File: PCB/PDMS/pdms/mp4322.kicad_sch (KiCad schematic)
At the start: 17 parts, among them U7 MP4322GDE-P

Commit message: WIP PCB folder structure and schematic clean-up
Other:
- company: (none) -> PGRacing Team
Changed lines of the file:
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@@
 (kicad_sch (version 20211123) (generator eeschema)
   (paper "A4")
+  (title_block
+    (rev "V4.2")
+    (company "PGRacing Team")
+    (comment 1 "Karol Pergoł")
+  )
   (junction (at 106.68 83.185) (diameter 0) (color 0 0 0 0)
   )

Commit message: PDMS PCB input modification WIP - no supply
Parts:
- C25, C26: value 0.1uF -> 100nF

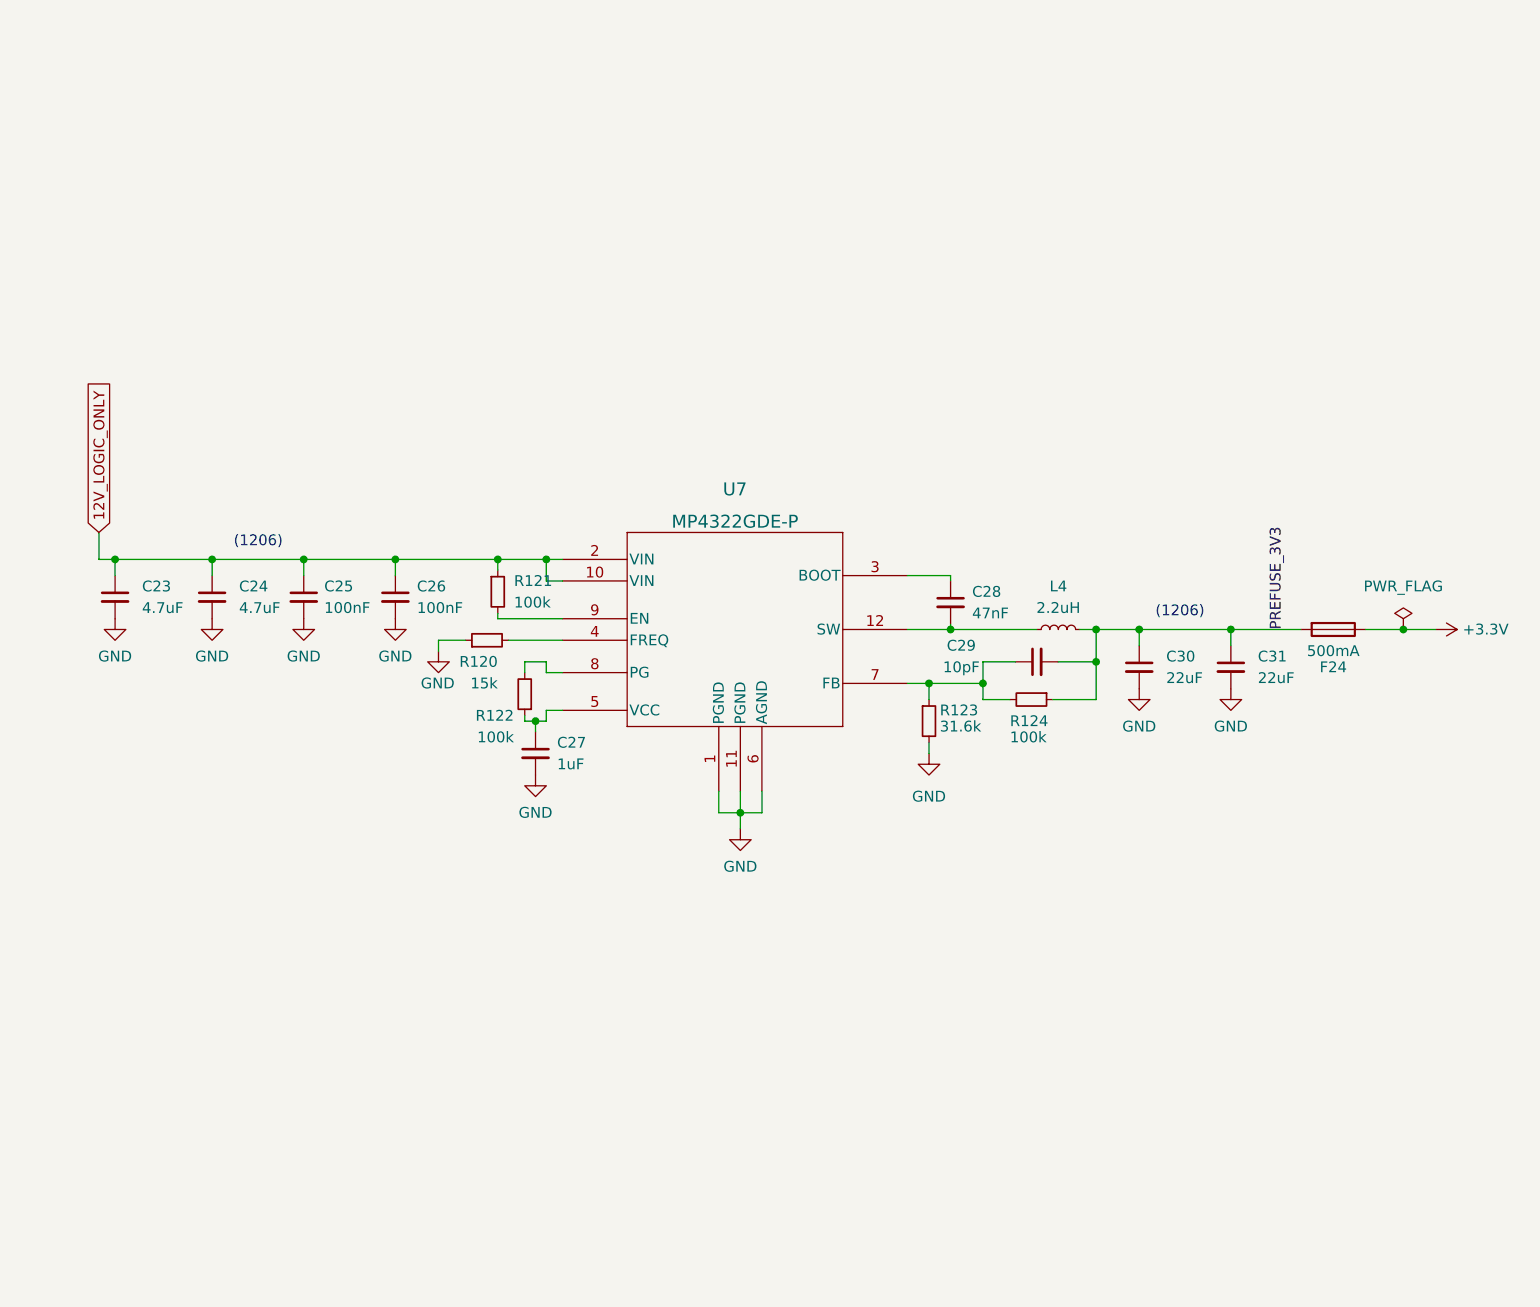
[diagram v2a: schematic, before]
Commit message: Fixed memory and aux routing, fixed decoupling of MCU, fixed hse oscilator layout, fixed BTS500 input capacitors size and thermal, fixed via stiching on output channels, changed LP mos  traces to thiner ones, WIP mp4322 layout repliacte
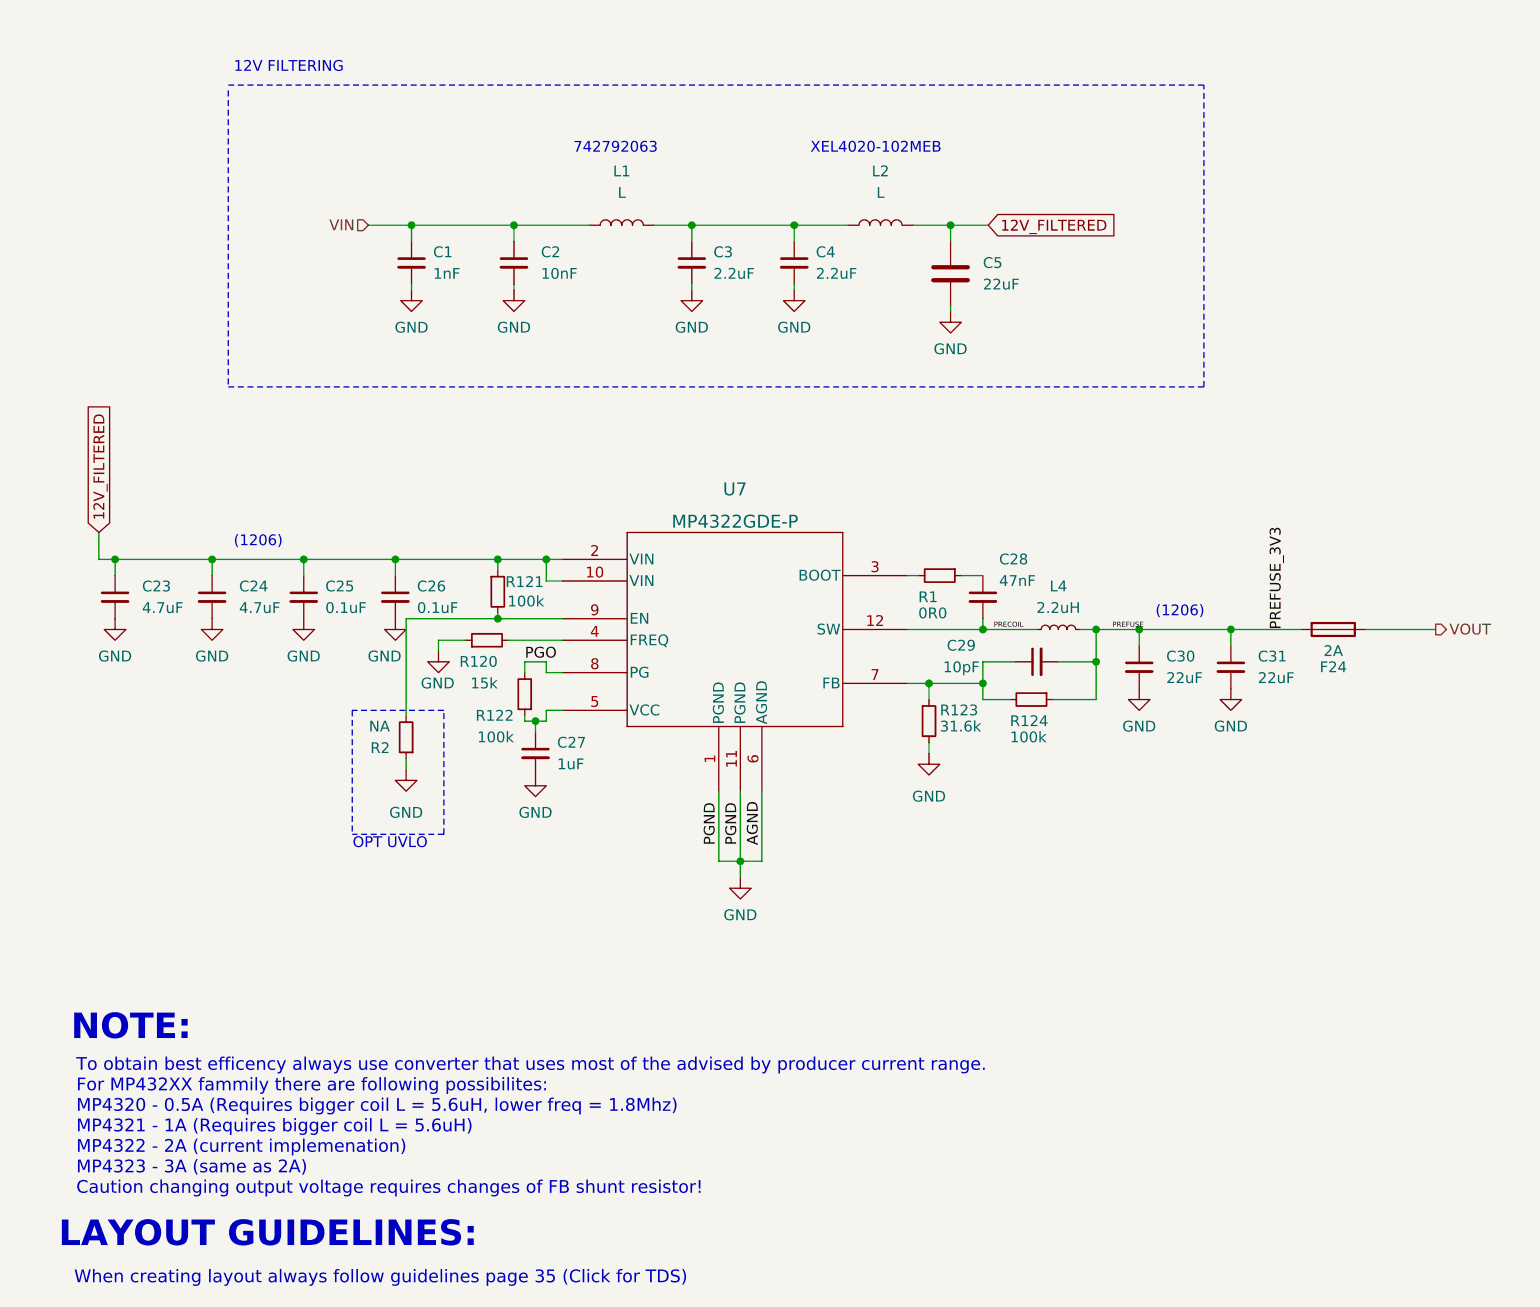
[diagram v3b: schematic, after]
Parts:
- added C1: 1nF, Capacitor_SMD:C_0402_1005Metric, symbol Device:C_Small
- added C2: 10nF, Capacitor_SMD:C_0402_1005Metric, symbol Device:C_Small
- added C3, C4: 2.2uF, Capacitor_SMD:C_0805_2012Metric, symbol Device:C_Small
- added C5: 22uF, Capacitor_SMD:CP_Elec_6.3x9.9, symbol Device:C
- added L1: L, Inductor_SMD:L_0805_2012Metric, symbol Device:L
- added L2: L, Inductor_SMD:L_Coilcraft_XxL4020, symbol Device:L
- added R1: 0R0, Resistor_SMD:R_0402_1005Metric, symbol Device:R_Small
- added R2: NA, Resistor_SMD:R_0402_1005Metric, symbol Device:R_Small
- C25, C26: value 100nF -> 0.1uF
- C27, C28, C29: footprint Resistor_SMD:R_0402_1005Metric -> Capacitor_SMD:C_0402_1005Metric
- F24: value 500mA -> 2A
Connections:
- net GND: now also C1.2, C2.2, C3.2, C4.2, C5.2, R2.1
- net PGO: now reaches R122.2, U7.8 (PG)
- net at R121.2, U7.9 (EN): now also R2.2
- net PRECOIL: now reaches C28.2, L4.1, U7.12 (SW)
- net at U7.3 (BOOT): now also R1.2; no longer C28.1
- net +3.3V renamed VOUT
- net 12V_LOGIC_ONLY renamed 12V_FILTERED
- net 12V_FILTERED: now also C5.1, L2.1
- net PREFUSE_3V3 renamed PREFUSE
- new net: C3.1, C4.1, L1.2, L2.2
- new net: C28.1, R1.1
- new net VIN: C1.1, C2.1, L1.1
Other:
- note added: "12V FILTERING"
- note added: "742792063"
- note added: "LAYOUT GUIDELINES:"
- note added: "NOTE:"
- note added: "OPT UVLO"
- note added: "To obtain best efficency always use converter that uses most of the advised by producer current range. For MP432XX fammily there are following possibilites: MP4320 - 0.5A (Requires bigger coil L = 5.6uH, lower freq = 1.8Mhz) MP4321 - 1A (Requires bigger coil L = 5.6uH) MP4322 - 2A (current implemenation) MP4323 - 3A (same as 2A) Caution changing output voltage requires changes of FB shunt resisto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"
- note added: "When creating layout always follow guidelines page 35 (Click for TDS)"
- note added: "XEL4020-102MEB"
- title: (none) -> MP432X Power section
- moved on the sheet: C28

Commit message: PDMS PCB WIP modification mp4322 finished layput, cleared USB-C layout, moved OSC32 for better fit
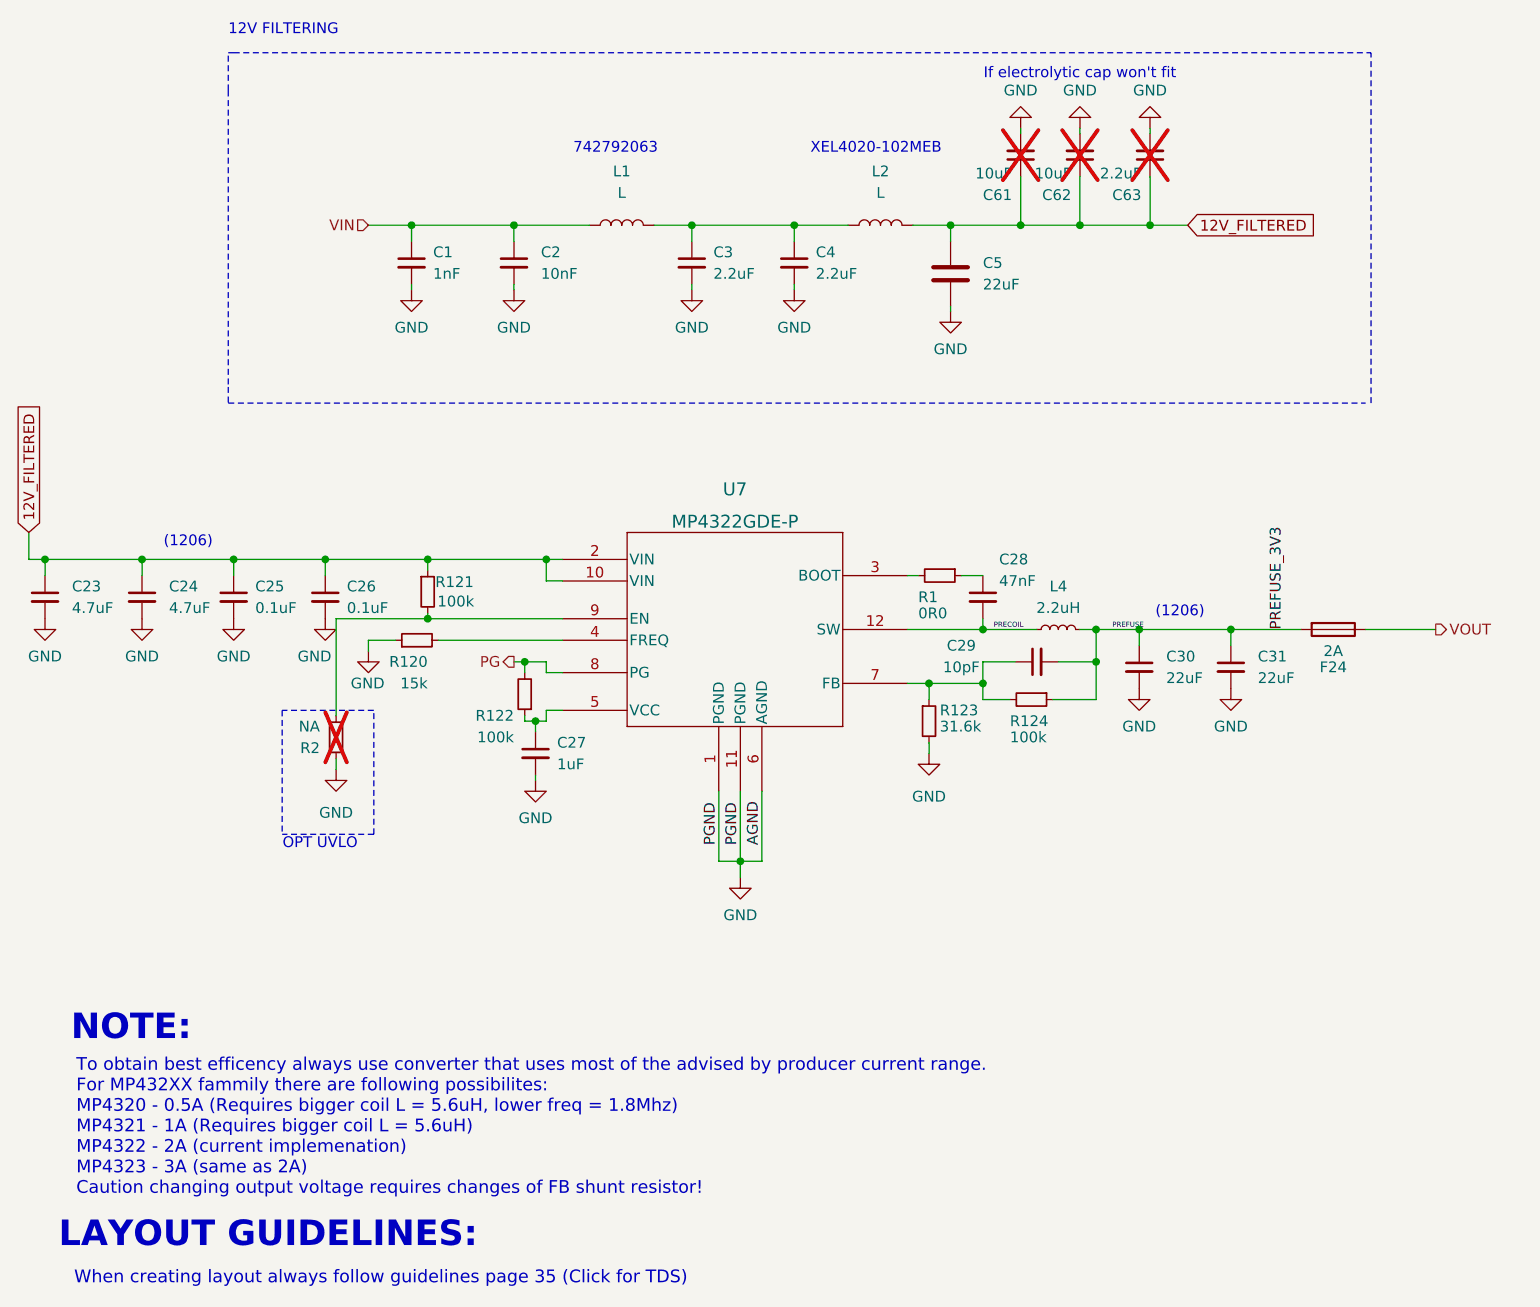
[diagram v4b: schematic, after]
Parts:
- added C61, C62: 10uF, Capacitor_SMD:C_1206_3216Metric, symbol Device:C_Small
- added C63: 2.2uF, Capacitor_SMD:C_1206_3216Metric, symbol Device:C_Small
- R2: now not fitted
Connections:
- net 12V_FILTERED: now also C61.1, C62.1, C63.1
- net GND: now also C61.2, C62.2, C63.2
- net PGO renamed PG
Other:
- note added: "If electrolytic cap won't fit"
- moved on the sheet: C23, C24, C25, C26, R120, R121

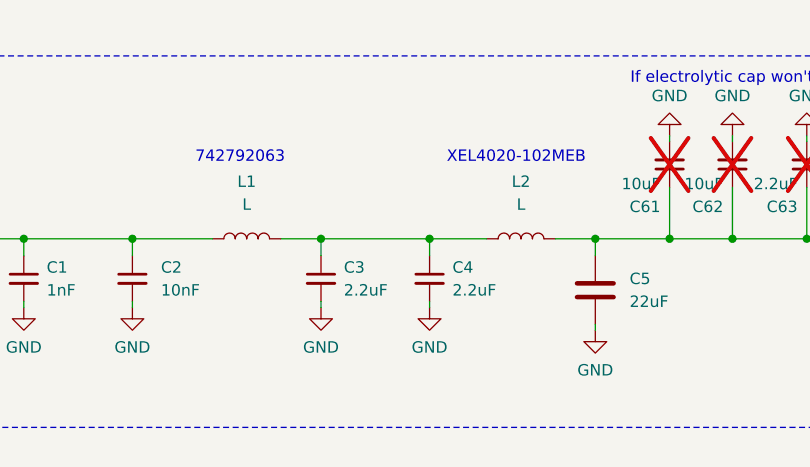
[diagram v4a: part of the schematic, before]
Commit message: PDMS PCB WIP modification - finished LDO layout
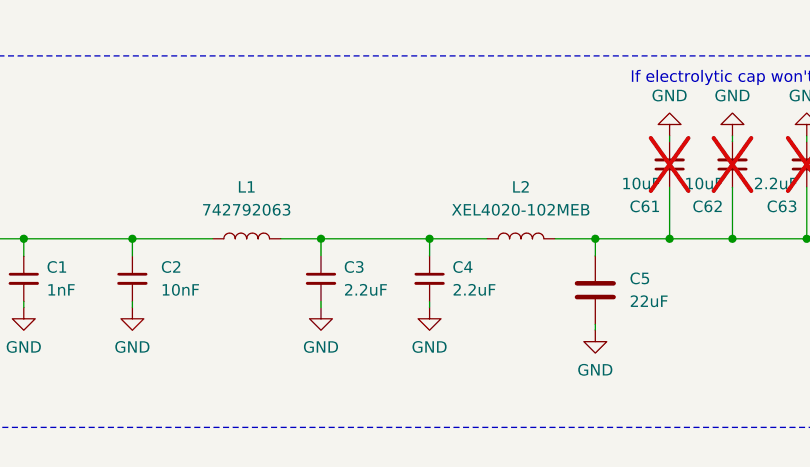
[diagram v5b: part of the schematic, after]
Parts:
- L1: value L -> 742792063
- L2: value L -> XEL4020-102MEB
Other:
- note removed: "742792063"
- note removed: "XEL4020-102MEB"
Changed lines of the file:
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@@
-		)
-	)
-	(text "XEL4020-102MEB"
-		(exclude_from_sim no)
-		(at 155.575 35.56 0)
-		(effects
-			(font
-				(size 1.27 1.27)
-			)
-			(justify left bottom)
 		)
 	)
@@
 			(justify left)
 			(href "https://www.monolithicpower.com/en/documentview/productdocument/index/version/2/document_type/Datasheet/lang/en/sku/MP4323GDE/document_id/10143/")
-		)
-	)
-	(text "742792063"
-		(exclude_from_sim no)
-		(at 127.635 35.56 0)
-		(effects
-			(font
-				(size 1.27 1.27)
-			)
-			(justify left bottom)
 		)
 	)
@@
 		(fields_autoplaced yes)
 		(property "Reference" "L1"
-			(at 133.35 37.465 90)
-			(effects
-				(font
-					(size 1.27 1.27)
-				)
-			)
-		)
-		(property "Value" "L"
-			(at 133.35 40.005 90)
+			(at 133.35 38.1 90)
+			(effects
+				(font
+					(size 1.27 1.27)
+				)
+			)
+		)
+		(property "Value" "742792063"
+			(at 133.35 40.64 90)
 			(effects
 				(font
@@
 		(fields_autoplaced yes)
 		(property "Reference" "L2"
-			(at 163.83 37.465 90)
-			(effects
-				(font
-					(size 1.27 1.27)
-				)
-			)
-		)
-		(property "Value" "L"
-			(at 163.83 40.005 90)
-			(effects
-				(font
+			(at 163.83 38.1 90)
+			(effects
+				(font
+					(size 1.27 1.27)
+				)
+			)
+		)
+		(property "Value" "XEL4020-102MEB"
+			(at 163.83 40.64 90)
+			(effects
+				(font
